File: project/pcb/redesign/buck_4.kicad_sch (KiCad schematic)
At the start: 13 parts, among them J3 NUCLEO-L432KC EXT USB

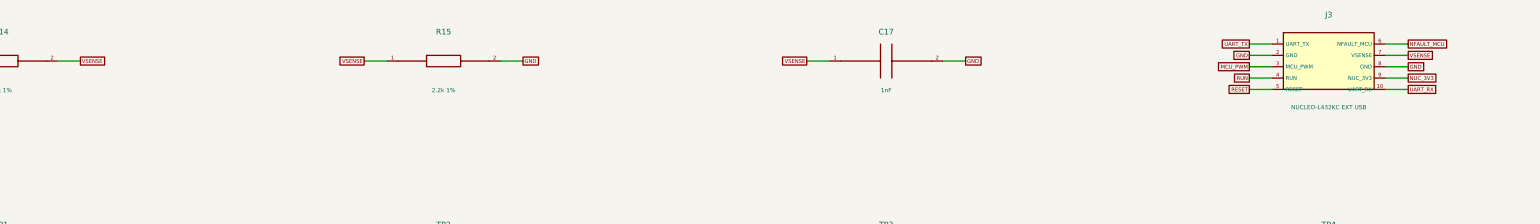
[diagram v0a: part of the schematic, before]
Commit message: feat: Buck PCB Rev B prototype package for JLCPCB
Rev B of project/pcb/redesign, prepared for a JLCPCB top-side SMT quote
and still pending bring-up. Rev A is preserved in history/revA_quote_20261027.

- Lands taken from manufacturer drawings (Murata 6000B, Same Sky TB002,
  Wurth WR-BHD, Panasonic SVPF/SVF, TA-I RLP, TI PW/DBV/DBZ/D/DBV5, Diodes
  SOD323); Q1 hole 1.4 mm per IPC-2222; U5 courtyard added.
- Power-domain interface: SN74LV4T125 buffer for PWM/RUN/RESET from +5V,
  TMUX1511 on the ADC path, TPS3808G33 supervisor, LM4040 2.5 V reference
  with BAT54WS clamps, fault latch set while the interface is disabled.
- Re-laid board: compact switching cell, no vias on HO/GATE/BOOT/SW,
  Kelvin sensing from RS1 inner edges, GND pours on both layers.
- L432KC firmware: Rev B ADC scale (6.4844 mV/count), VOUT-collapse fault,
  host test.
- Fabrication package production/jlcpcb-revB-2026-10-27: DRC 0 errors,
  0 unconnected, 0 parity; ERC 0 errors.

Not ready to order: L1/L2 have no JLC/LCSC stock, the LM4040 X-variant and
R10 supply need decisions, the JLC viewer rotation check and ARM build are
pending. BUCK_BOARD_REVIEWED stays 0. See revB_release_report.md.

Co-Authored-By: Claude Opus 5.5 <noreply@anthropic.com>
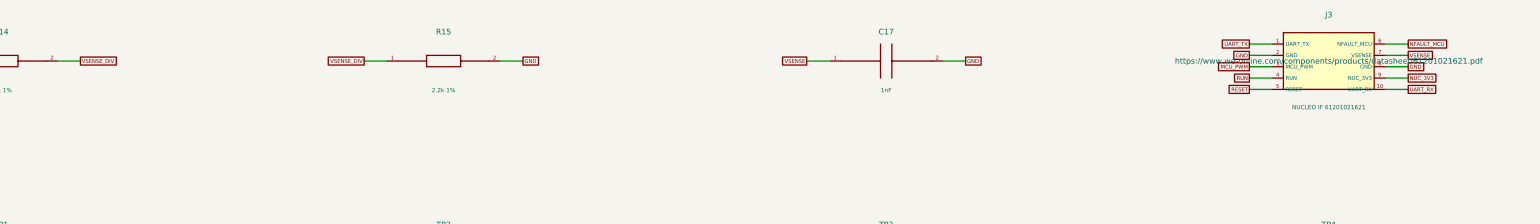
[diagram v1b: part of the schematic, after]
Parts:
- J3: value NUCLEO-L432KC EXT USB -> NUCLEO IF 61201021621; footprint Connector_IDC:IDC-Header_2x05_P2.54mm_Vertical -> Buck_RevB:Wurth_WR-BHD_61201021621_2x05_P2.54mm_Vertical; Assembly NUCLEO external; NOT assembled by JLCPCB; header MPN/land p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 -> MANUAL_THT; Electrical_Approval PENDING - NOT APPROVED -> PENDING - PROTOTYPE BRING-UP; NOT ELECTRICALLY VALIDATED; LCSC NOT SELECTED -> C4355000; MPN TBD keyed IDC header 2x5 2.54mm -> 61201021621; Manufacturer TBD -> Wurth Elektronik; Migration_Notes External NUCLEO powered via USB. No Buck 5V/VIN connection.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 -> Rev B: J3 signals pass through U7/U8; NUC_3V3 powers U8 and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; Migration_Status NUCLEO UPDATE - USER ACCEPTED NOMINAL CHANGE; ELECTRICAL RE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 -> REV B - PART FIXED BY RELEASE PLAN
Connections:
- net VSENSE: no longer R14.2, R15.1
- new net VSENSE_DIV: R14.2, R15.1
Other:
- title: STM32 interface and test points - REV A / HOLD FABRICATION -> STM32 interface and test points - REV B PROTOTYPE
